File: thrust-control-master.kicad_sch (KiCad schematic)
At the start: 0 parts

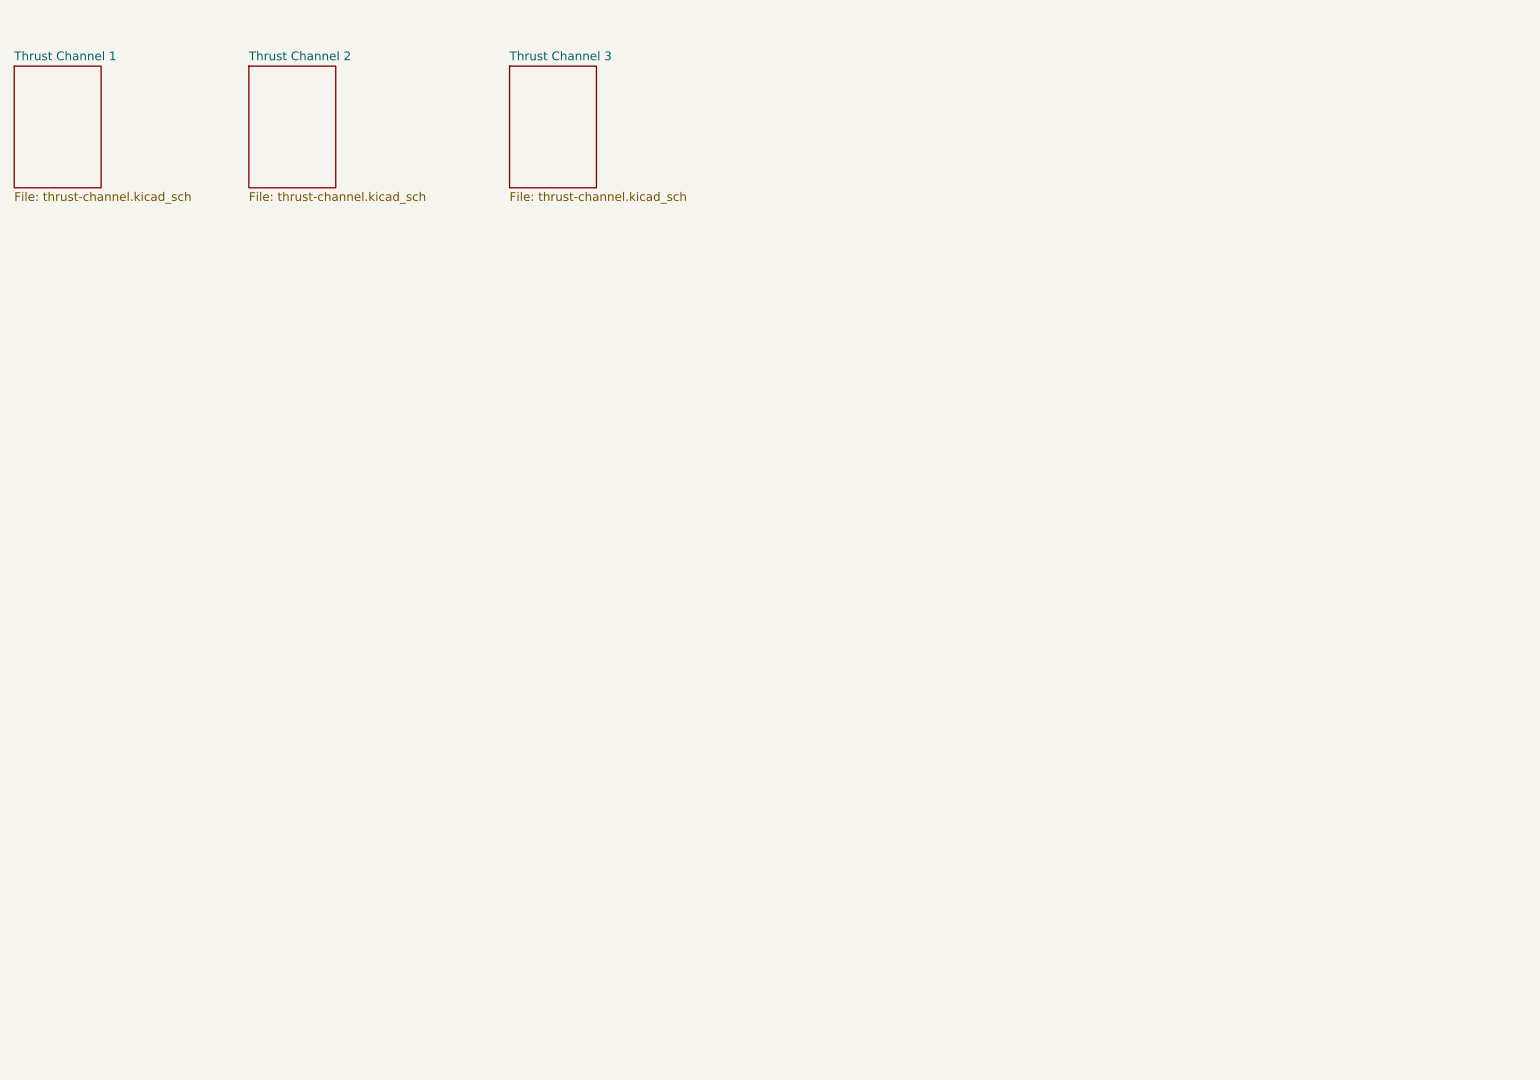
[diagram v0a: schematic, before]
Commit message: convert thrust control
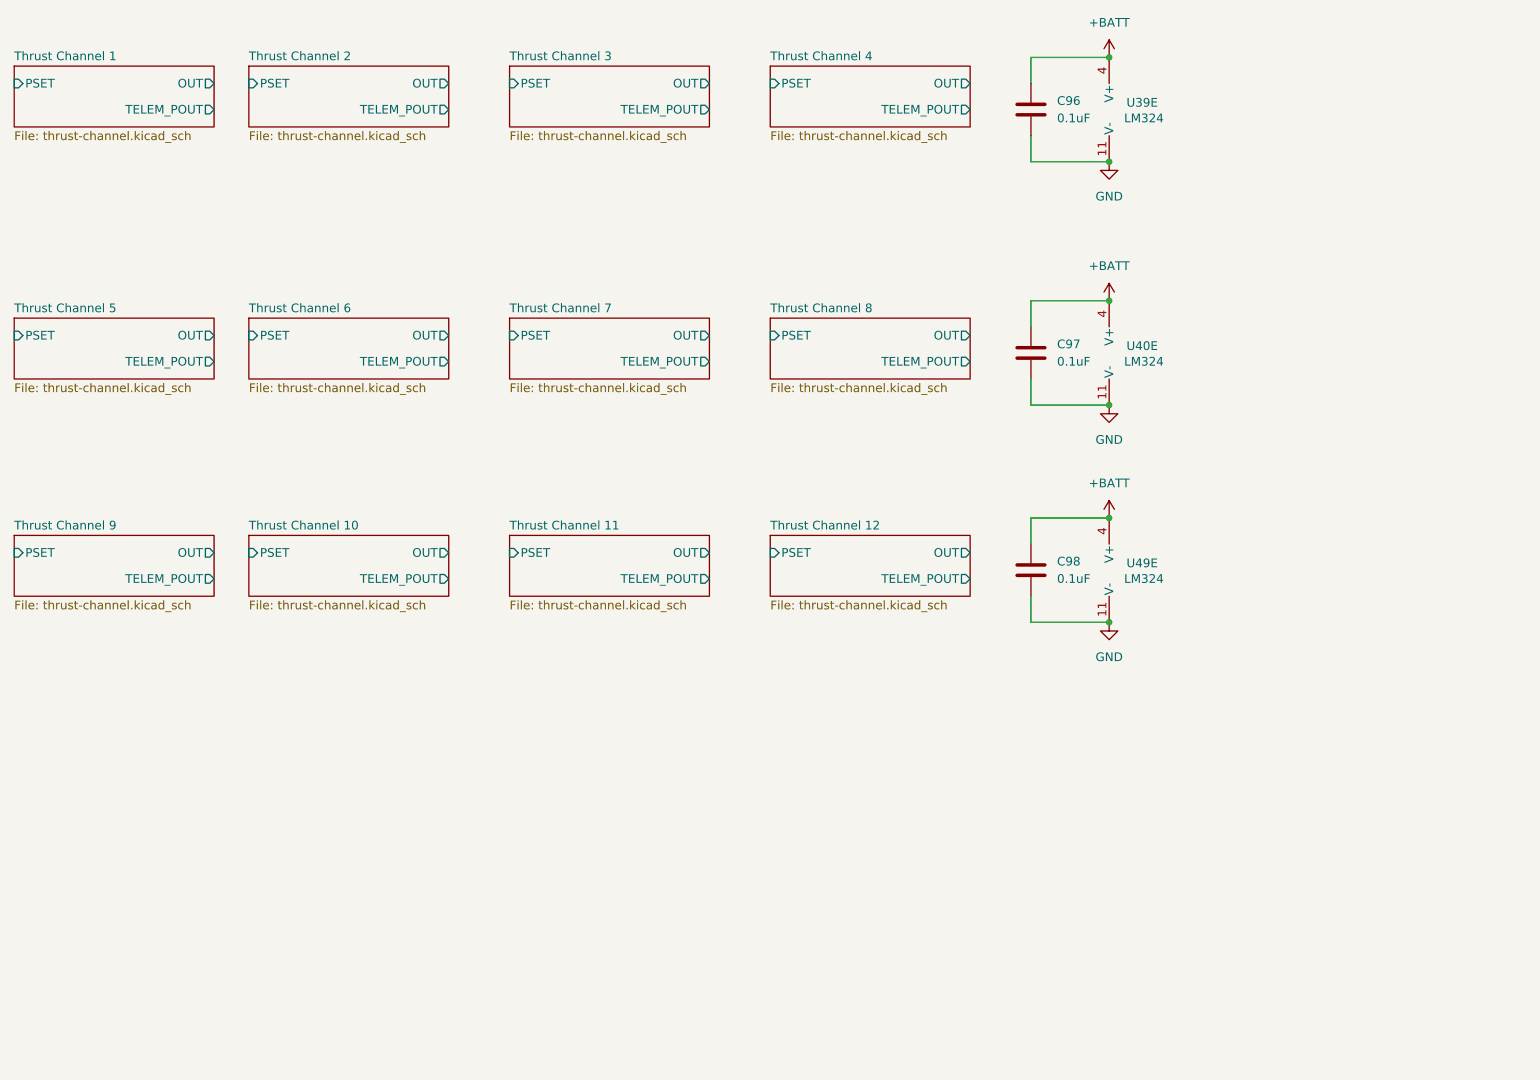
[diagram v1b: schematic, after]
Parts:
- added C96, C97, C98: 0.1uF, symbol Device:C
- added U39, U40, U49: LM324, symbol Amplifier_Operational:LM324
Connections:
- new net +BATT: C96.1, C97.1, C98.1, U39.4 (V+), U40.4 (V+), U49.4 (V+)
- new net GND: C96.2, C97.2, C98.2, U39.11 (V-), U40.11 (V-), U49.11 (V-)
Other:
- added sheet Thrust Channel 10 (thrust-channel.kicad_sch)
- added sheet Thrust Channel 11 (thrust-channel.kicad_sch)
- added sheet Thrust Channel 12 (thrust-channel.kicad_sch)
- added sheet Thrust Channel 4 (thrust-channel.kicad_sch)
- added sheet Thrust Channel 5 (thrust-channel.kicad_sch)
- added sheet Thrust Channel 6 (thrust-channel.kicad_sch)
- added sheet Thrust Channel 7 (thrust-channel.kicad_sch)
- added sheet Thrust Channel 8 (thrust-channel.kicad_sch)
- added sheet Thrust Channel 9 (thrust-channel.kicad_sch)
- sheet Thrust Channel 1 ports: added OUT, PSET, TELEM_POUT; removed none
- sheet Thrust Channel 2 ports: added OUT, PSET, TELEM_POUT; removed none
- sheet Thrust Channel 3 ports: added OUT, PSET, TELEM_POUT; removed none

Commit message: work
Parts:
- renumbered C96 to C81, C97 to C82, C98 to C83, U39 to U33, U40 to U34, U49 to U35
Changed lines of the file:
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@@
 		(dnp no)
 		(fields_autoplaced yes)
-		(property "Reference" "C98"
+		(property "Reference" "C83"
 			(at 177.8 101.5999 0)
 			(effects
@@
 			(project "femta-control"
 				(path "/838bf11c-36b7-41d7-9462-fe98a188d617/3bf849ef-bca6-4864-a347-fbff558d0891"
-					(reference "C98")
+					(reference "C83")
 					(unit 1)
 				)
@@
 		(on_board yes)
 		(dnp no)
-		(property "Reference" "U39"
+		(property "Reference" "U33"
 			(at 190.246 34.544 0)
 			(effects
@@
 			(project "femta-control"
 				(path "/838bf11c-36b7-41d7-9462-fe98a188d617/3bf849ef-bca6-4864-a347-fbff558d0891"
-					(reference "U39")
+					(reference "U33")
 					(unit 5)
 				)
@@
 		(dnp no)
 		(fields_autoplaced yes)
-		(property "Reference" "#PWR0249"
+		(property "Reference" "#PWR0150"
 			(at 185.42 116.84 0)
 			(effects
@@
 			(project "femta-control"
 				(path "/838bf11c-36b7-41d7-9462-fe98a188d617/3bf849ef-bca6-4864-a347-fbff558d0891"
-					(reference "#PWR0249")
+					(reference "#PWR0150")
 					(unit 1)
 				)
@@
 		(dnp no)
 		(fields_autoplaced yes)
-		(property "Reference" "#PWR0206"
+		(property "Reference" "#PWR0146"
 			(at 185.42 49.53 0)
 			(effects
@@
 			(project "femta-control"
 				(path "/838bf11c-36b7-41d7-9462-fe98a188d617/3bf849ef-bca6-4864-a347-fbff558d0891"
-					(reference "#PWR0206")
+					(reference "#PWR0146")
 					(unit 1)
 				)
@@
 		(on_board yes)
 		(dnp no)
-		(property "Reference" "U49"
+		(property "Reference" "U35"
 			(at 190.246 101.854 0)
 			(effects
@@
 			(project "femta-control"
 				(path "/838bf11c-36b7-41d7-9462-fe98a188d617/3bf849ef-bca6-4864-a347-fbff558d0891"
-					(reference "U49")
+					(reference "U35")
 					(unit 5)
 				)
@@
 		(dnp no)
 		(fields_autoplaced yes)
-		(property "Reference" "#PWR0211"
+		(property "Reference" "#PWR0148"
 			(at 185.42 85.09 0)
 			(effects
@@
 			(project "femta-control"
 				(path "/838bf11c-36b7-41d7-9462-fe98a188d617/3bf849ef-bca6-4864-a347-fbff558d0891"
-					(reference "#PWR0211")
+					(reference "#PWR0148")
 					(unit 1)
 				)
@@
 		(on_board yes)
 		(dnp no)
-		(property "Reference" "U40"
+		(property "Reference" "U34"
 			(at 190.246 70.104 0)
 			(effects
@@
 			(project "femta-control"
 				(path "/838bf11c-36b7-41d7-9462-fe98a188d617/3bf849ef-bca6-4864-a347-fbff558d0891"
-					(reference "U40")
+					(reference "U34")
 					(unit 5)
 				)
@@
 		(dnp no)
 		(fields_autoplaced yes)
-		(property "Reference" "C96"
+		(property "Reference" "C81"
 			(at 177.8 34.2899 0)
 			(effects
@@
 			(project "femta-control"
 				(path "/838bf11c-36b7-41d7-9462-fe98a188d617/3bf849ef-bca6-4864-a347-fbff558d0891"
-					(reference "C96")
+					(reference "C81")
 					(unit 1)
 				)
@@
 		(dnp no)
 		(fields_autoplaced yes)
-		(property "Reference" "C97"
+		(property "Reference" "C82"
 			(at 177.8 69.8499 0)
 			(effects
@@
 			(project "femta-control"
 				(path "/838bf11c-36b7-41d7-9462-fe98a188d617/3bf849ef-bca6-4864-a347-fbff558d0891"
-					(reference "C97")
+					(reference "C82")
 					(unit 1)
 				)
@@
 		(dnp no)
 		(fields_autoplaced yes)
-		(property "Reference" "#PWR0205"
+		(property "Reference" "#PWR0145"
 			(at 185.42 31.75 0)
 			(effects
@@
 			(project "femta-control"
 				(path "/838bf11c-36b7-41d7-9462-fe98a188d617/3bf849ef-bca6-4864-a347-fbff558d0891"
-					(reference "#PWR0205")
+					(reference "#PWR0145")
 					(unit 1)
 				)
@@
 		(dnp no)
 		(fields_autoplaced yes)
-		(property "Reference" "#PWR0248"
+		(property "Reference" "#PWR0149"
 			(at 185.42 99.06 0)
 			(effects
@@
 			(project "femta-control"
 				(path "/838bf11c-36b7-41d7-9462-fe98a188d617/3bf849ef-bca6-4864-a347-fbff558d0891"
-					(reference "#PWR0248")
+					(reference "#PWR0149")
 					(unit 1)
 				)
@@
 		(dnp no)
 		(fields_autoplaced yes)
-		(property "Reference" "#PWR0207"
+		(property "Reference" "#PWR0147"
 			(at 185.42 67.31 0)
 			(effects
@@
 			(project "femta-control"
 				(path "/838bf11c-36b7-41d7-9462-fe98a188d617/3bf849ef-bca6-4864-a347-fbff558d0891"
-					(reference "#PWR0207")
+					(reference "#PWR0147")
 					(unit 1)
 				)

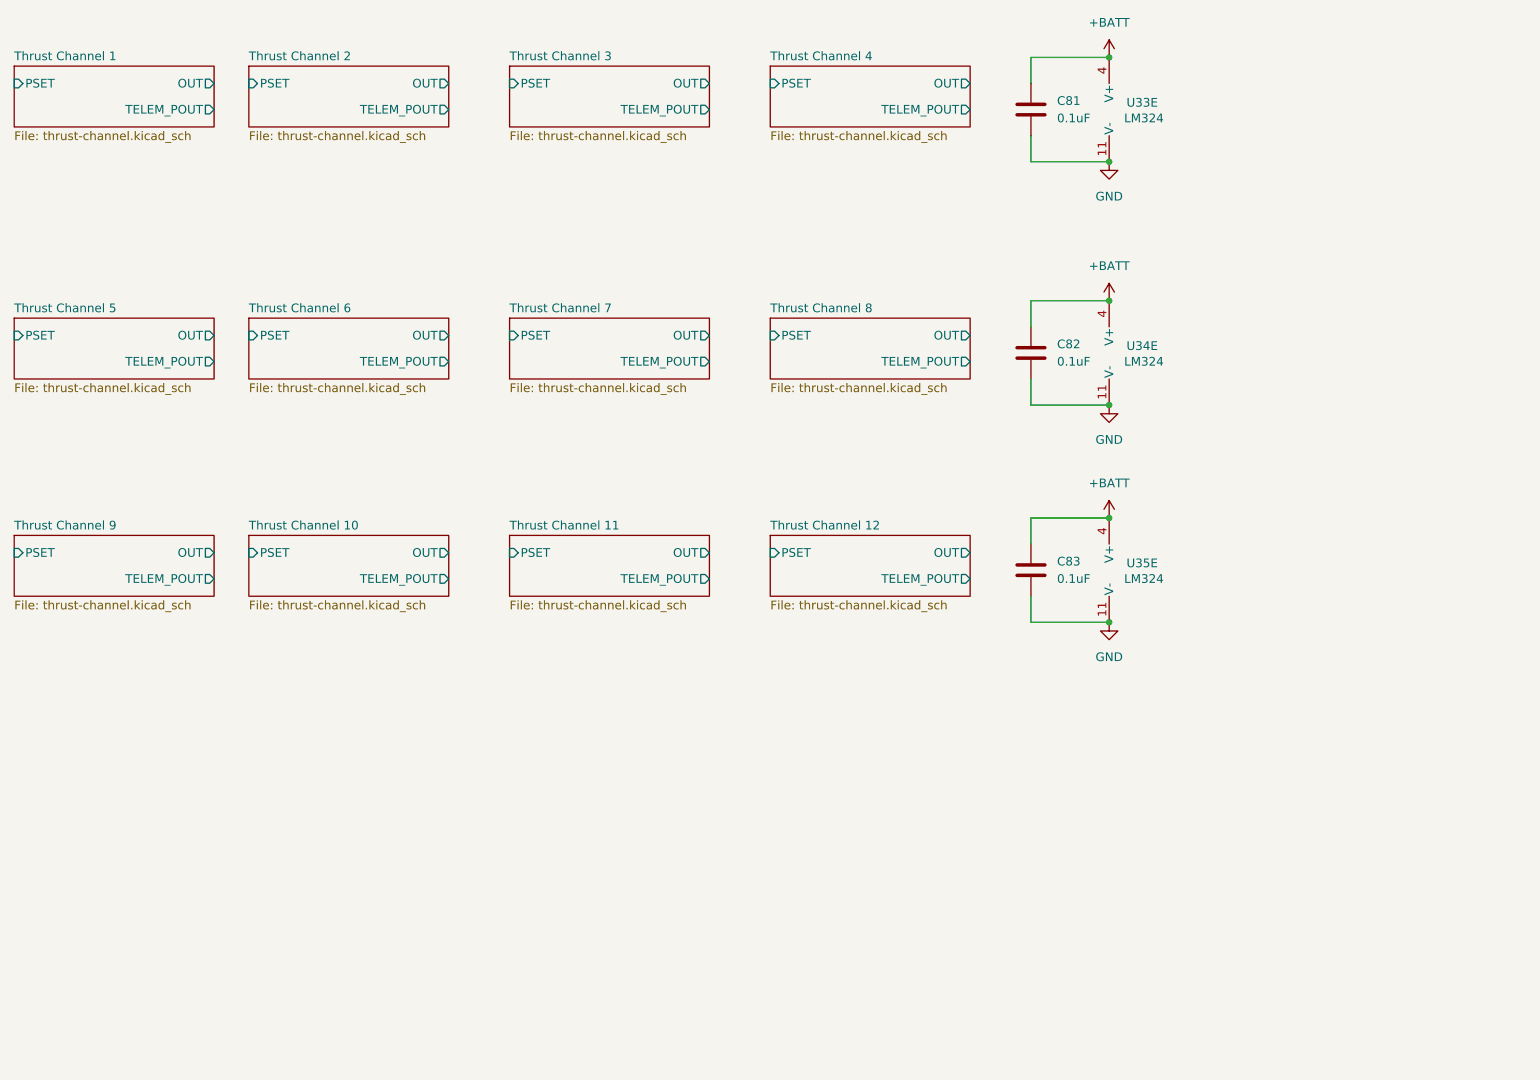
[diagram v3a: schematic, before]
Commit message: thrust control
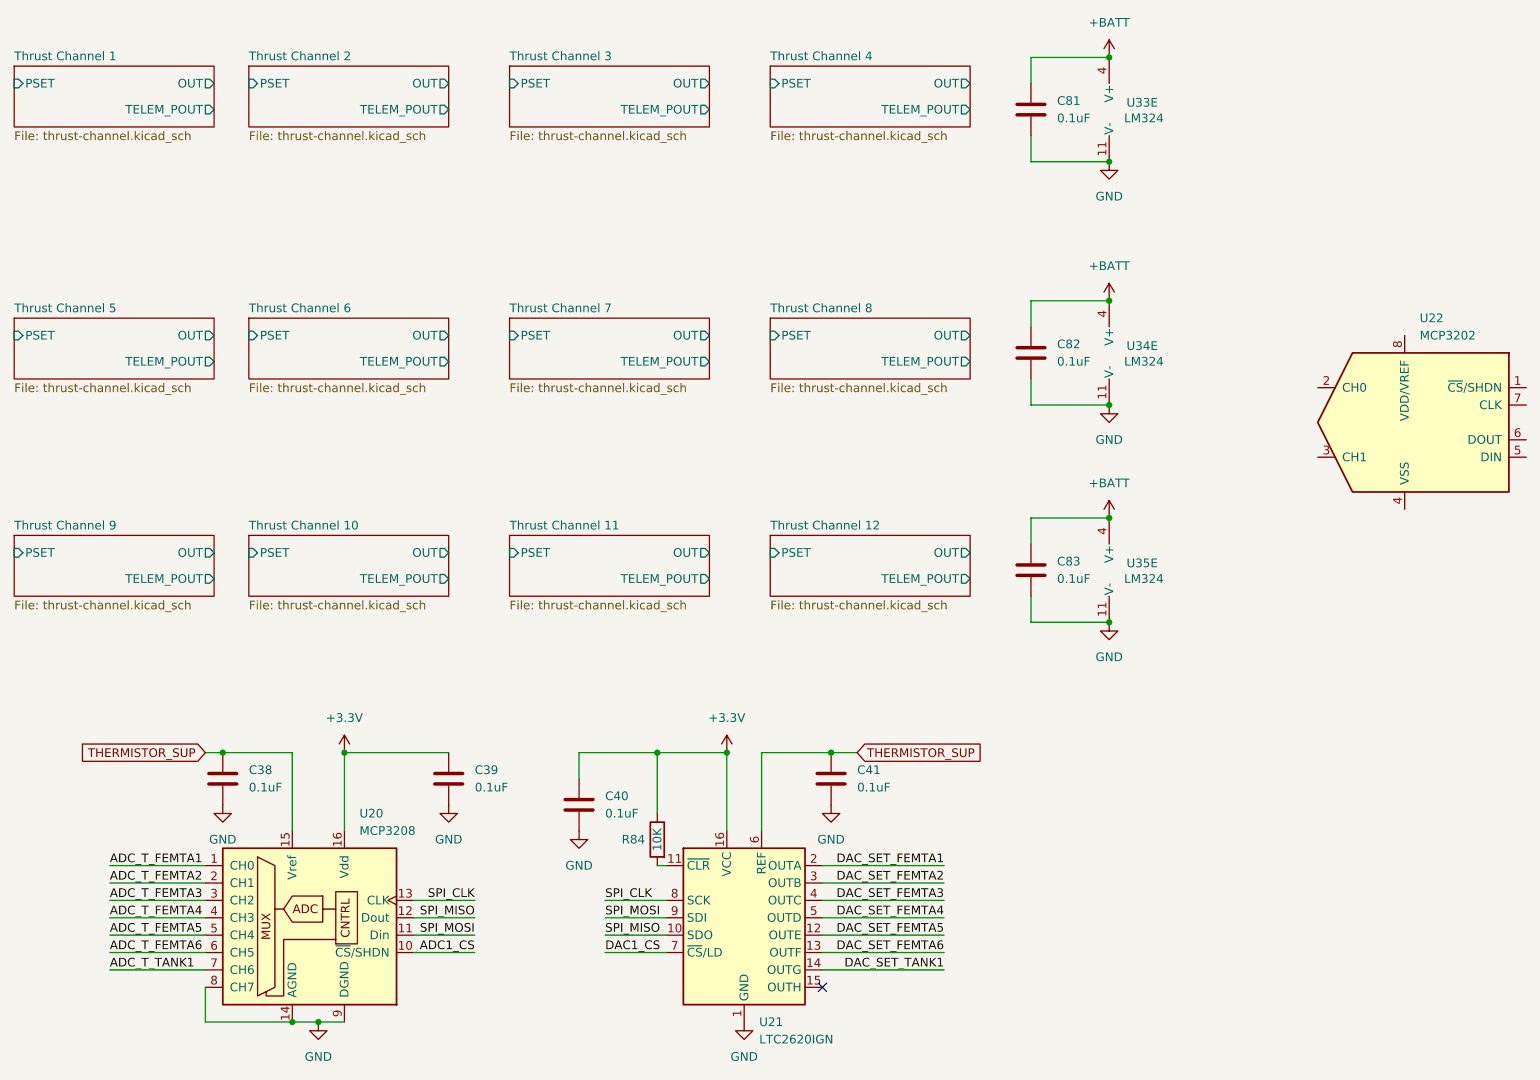
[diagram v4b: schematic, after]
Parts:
- added C38, C39, C40, C41: 0.1uF, symbol Device:C
- added R84: 10K, symbol Device:R
- added U20: MCP3208, Package_SO:SOIC-16_3.9x9.9mm_P1.27mm, symbol Analog_ADC:MCP3208
- added U21: LTC2620IGN, symbol femta-control-custom:LTC2620IGN
- added U22: MCP3202, symbol Analog_ADC:MCP3202
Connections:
- net GND: now also C38.2, C39.2, C40.2, C41.2, U20.14 (AGND), U20.8 (CH7), U20.9 (DGND), U21.1 (GND)
- new net: R84.2, U21.11 (~{CLR})
- new net +3.3V: C39.1, C40.1, R84.1, U20.16 (Vdd), U21.16 (VCC)
- new net ADC1_CS: U20.10 (~{CS}/SHDN)
- new net ADC_T_FEMTA1: U20.1 (CH0)
- new net ADC_T_FEMTA2: U20.2 (CH1)
- new net ADC_T_FEMTA3: U20.3 (CH2)
- new net ADC_T_FEMTA4: U20.4 (CH3)
- new net ADC_T_FEMTA5: U20.5 (CH4)
- new net ADC_T_FEMTA6: U20.6 (CH5)
- new net ADC_T_TANK1: U20.7 (CH6)
- new net DAC1_CS: U21.7 (~{CS}/LD)
- new net DAC_SET_FEMTA1: U21.2 (OUTA)
- new net DAC_SET_FEMTA2: U21.3 (OUTB)
- new net DAC_SET_FEMTA3: U21.4 (OUTC)
- new net DAC_SET_FEMTA4: U21.5 (OUTD)
- new net DAC_SET_FEMTA5: U21.12 (OUTE)
- new net DAC_SET_FEMTA6: U21.13 (OUTF)
- new net DAC_SET_TANK1: U21.14 (OUTG)
- new net SPI_CLK: U20.13 (CLK), U21.8 (SCK)
- new net SPI_MISO: U20.12 (Dout), U21.10 (SDO)
- new net SPI_MOSI: U20.11 (Din), U21.9 (SDI)
- new net THERMISTOR_SUP: C38.1, C41.1, U20.15 (Vref), U21.6 (REF)
- no-connect marks 0 -> 1
